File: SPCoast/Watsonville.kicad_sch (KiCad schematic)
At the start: 201 parts, among them SW15003 3, SW15005 5, SW15007 7, SW15009 9, SW15011 11, SW15013 13, SW15015 15, SW15017 17, SW15019 19, SW15021 21, SW15023 23, SW15025 25, SW15837 837

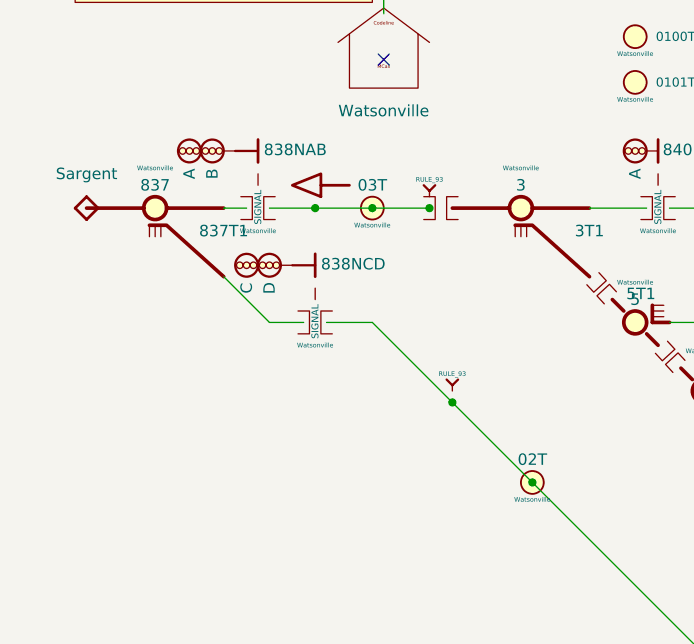
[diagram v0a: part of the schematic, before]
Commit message: feat(kicad): owner edit (2026-10-26): NextCP carries Interlocking; Industry carries Name; HBA leaves the track
The owner's edits after the trackplan review:
- NextCP gains Interlocking = ${Value}, a key the compiler reads for the destination; every instance takes it.
  Christopher's two NextCPs toward Corporal now say Corporal (both said Sargent).
- Industry gains Name = ${VALUE}. The five Industries are named: Gilroy Industry at Luchessa, Beet Loader 1
  and 2 at Corporal and at Sargent.
- Sargent's HBA (hot box alarm) is moved off 1SAT's net; its MC pin is unconnected and it carries Milepost 83.4.
- Watsonville: one Rule 93 (YARD) symbol is moved to the yard side of its joint.
Panels/ is left untracked.

Verified:
- Netlist exported by the owner 2026-10-26 12:37, newer than every sheet and the library.
- lint_symbol_fields: 100 symbols, 0 errors, 0 warnings.

Co-Authored-By: Claude Opus 5.5 <noreply@anthropic.com>
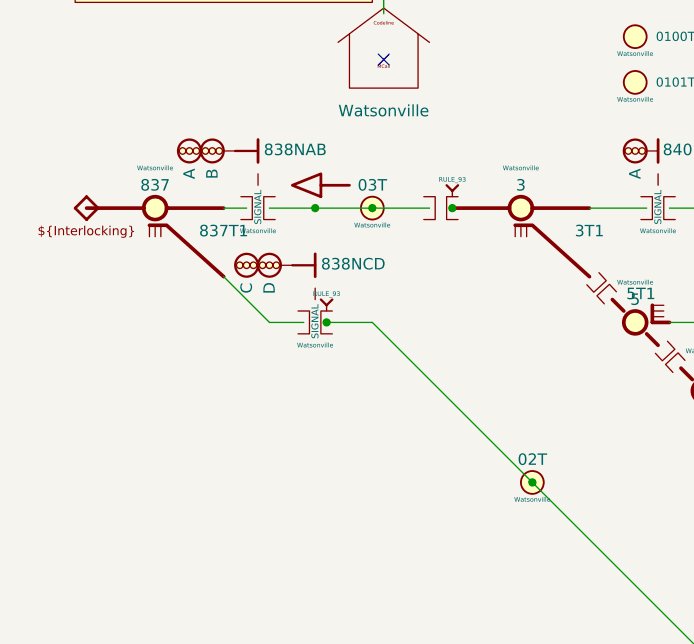
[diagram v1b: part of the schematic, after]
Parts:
- CP15001: Interlocking (none) -> ${Value}
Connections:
- net at B15003.2 (B), B15004.1 (A), DOT15004.1 (To)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: no longer DOT15001.1 (To)
- net at B15004.2 (B), SW15003.1 (C): now also DOT15001.1 (To)

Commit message: feat(kicad): owner edit (2026-10-27): Watsonville gets mast 838SAB on a new signal joint
The owner added the southbound 838SAB mast (a double mast with heads A and B), on
a new IRJ-Signal joint with CP Watsonville, closing the 838S TBD. The desk's 838
signal lever now has a field mast. The Sargent NextCP was redrawn, and
SPCoast.kicad_pro records the new designators.

Verified: only Watsonville.kicad_sch and SPCoast.kicad_pro changed. The added
symbols are Mast_Double 838SAB (Style double), heads A and B (CPL) and IRJ-Signal
B15005 (CP Watsonville); NextCP CP15001 (Sargent) is unchanged in its fields.
KiCad was closed (no lock files).

Co-Authored-By: Claude Opus 5.5 <noreply@anthropic.com>
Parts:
- added B15005: (no value), symbol Railroad-Trackplan:IRJ-Signal
- added H15013: A, symbol Railroad-Trackplan:Signal Head - CPL
- added H15014: B, symbol Railroad-Trackplan:Signal Head - CPL
- added S15011: 838SAB, symbol Railroad-Trackplan:Mast_Double
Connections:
- net at CP15001.1 (To): now also B15005.2 (B); no longer SW15837.1 (C)
- new net: H15014.1 (M), S15011.2 (H2)
- new net: B15005.1 (A), SW15837.1 (C)
- new net: H15013.1 (M), S15011.3 (H1)
- new net: B15005.3 (SIGNAL), S15011.1 (SIGNAL)

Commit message: refactor(symbols): the CP field is CP Name on every trackplan symbol
One fact, which house an appliance or circuit stands in, had two field
names: CP Name on the House and PanelColumn, CP on 17 trackplan
symbols. Every CP is now CP Name, in the library and in each placed
symbol, by a text rename of the field name only (KiCad's update
symbols was not used; it resets per-instance fields).

Verified: fresh kicad-cli netlists before and after: 754 components on
both, 136 had CP, every field identical once CP is read as CP Name, no
CP left. lint_symbol_fields: 100 symbols, 0 errors, 0 warnings.

Co-Authored-By: Claude Opus 5.5 <noreply@anthropic.com>
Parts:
- B15002, B15003, B15005, B15012, B15013, B15014, B15015, B15016, B15017, B15018, B15043, FLK15003, FLK15004, SW15003, SW15005, SW15007, SW15009, SW15011, SW15013, SW15015, SW15017, SW15019, SW15021, SW15023, SW15025, SW15837, TC15001, TC15002, TC15003, TC15004, TC15005, TC15006, TC15007, TC15008, TC15009, TC15010, TC15011, TC15012, TC15013, TC15014, TC15015, TC15016, TC15017, TC15018, TC15019, TC15020, TC15021, TC15022, TC15023, TC15024, TC15025, TC15026, TC15027, TC15028, TC15029, TC15030, TC15031, TC15032, TC15033, TC15034: CP Watsonville -> (none); CP Name (none) -> Watsonville
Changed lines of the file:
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@@
 			)
 		)
-		(property "CP" "Watsonville"
+		(property "CP Name" "Watsonville"
 			(at 222.25 79.375 0)
 			(show_name no)
@@
 			)
 		)
-		(property "CP" "Watsonville"
+		(property "CP Name" "Watsonville"
 			(at 81.28 37.465 0)
 			(show_name no)
@@
 			)
 		)
-		(property "CP" "Watsonville"
+		(property "CP Name" "Watsonville"
 			(at 167.64 76.835 0)
 			(show_name no)
@@
 			)
 		)
-		(property "CP" "Watsonville"
+		(property "CP Name" "Watsonville"
 			(at 137.16 107.315 0)
 			(show_name no)
@@
 			)
 		)
-		(property "CP" "Watsonville"
+		(property "CP Name" "Watsonville"
 			(at 167.64 56.515 0)
 			(show_name no)
@@
 			)
 		)
-		(property "CP" "Watsonville"
+		(property "CP Name" "Watsonville"
 			(at 68.58 50.165 0)
 			(show_name no)
@@
 			)
 		)
-		(property "CP" "Watsonville"
+		(property "CP Name" "Watsonville"
 			(at 39.37 57.15 0)
 			(show_name no)
@@
 			)
 		)
-		(property "CP" "Watsonville"
+		(property "CP Name" "Watsonville"
 			(at 116.84 92.71 0)
 			(show_name no)
@@
 			)
 		)
-		(property "CP" "Watsonville"
+		(property "CP Name" "Watsonville"
 			(at 147.32 56.515 0)
 			(show_name no)
@@
 			)
 		)
-		(property "CP" "Watsonville"
+		(property "CP Name" "Watsonville"
 			(at 45.72 69.85 0)
 			(show_name no)
@@
 			)
 		)
-		(property "CP" "Watsonville"
+		(property "CP Name" "Watsonville"
 			(at 237.49 94.615 0)
 			(show_name no)
@@
 			)
 		)
-		(property "CP" "Watsonville"
+		(property "CP Name" "Watsonville"
 			(at 137.16 56.515 0)
 			(show_name no)
@@
 			)
 		)
-		(property "CP" "Watsonville"
+		(property "CP Name" "Watsonville"
 			(at 81.28 62.865 0)
 			(show_name no)
@@
 			)
 		)
-		(property "CP" "Watsonville"
+		(property "CP Name" "Watsonville"
 			(at 52.07 56.515 0)
 			(show_name no)
@@
 			)
 		)
-		(property "CP" "Watsonville"
+		(property "CP Name" "Watsonville"
 			(at 147.32 92.075 0)
 			(show_name no)
@@
 			)
 		)
-		(property "CP" "Watsonville"
+		(property "CP Name" "Watsonville"
 			(at 205.74 69.215 0)
 			(show_name no)
@@
 			)
 		)
-		(property "CP" "Watsonville"
+		(property "CP Name" "Watsonville"
 			(at 137.16 76.835 0)
 			(show_name no)
@@
 			)
 		)
-		(property "CP" "Watsonville"
+		(property "CP Name" "Watsonville"
 			(at 157.48 107.315 0)
 			(show_name no)
@@
 			)
 		)
-		(property "CP" "Watsonville"
+		(property "CP Name" "Watsonville"
 			(at 157.48 92.075 0)
 			(show_name no)
@@
 			)
 		)
-		(property "CP" "Watsonville"
+		(property "CP Name" "Watsonville"
 			(at 109.22 85.09 0)
 			(show_name no)
@@
 			)
 		)
-		(property "CP" "Watsonville"
+		(property "CP Name" "Watsonville"
 			(at 111.76 93.345 0)
 			(show_name no)
@@
 			)
 		)
-		(property "CP" "Watsonville"
+		(property "CP Name" "Watsonville"
 			(at 157.48 56.515 0)
 			(show_name no)
@@
 			)
 		)
-		(property "CP" "Watsonville"
+		(property "CP Name" "Watsonville"
 			(at 101.6 77.47 0)
 			(show_name no)
@@
 			)
 		)
-		(property "CP" "Watsonville"
+		(property "CP Name" "Watsonville"
 			(at 147.32 107.315 0)
 			(show_name no)
@@
 			)
 		)
-		(property "CP" "Watsonville"
+		(property "CP Name" "Watsonville"
 			(at 81.28 42.545 0)
 			(show_name no)
@@
 			)
 		)
-		(property "CP" "Watsonville"
+		(property "CP Name" "Watsonville"
 			(at 69.85 86.995 0)
 			(show_name no)
@@
 			)
 		)
-		(property "CP" "Watsonville"
+		(property "CP Name" "Watsonville"
 			(at 243.84 115.57 0)
 			(show_name no)
@@
 			)
 		)
-		(property "CP" "Watsonville"
+		(property "CP Name" "Watsonville"
 			(at 157.48 84.455 0)
 			(show_name no)
@@
 			)
 		)
-		(property "CP" "Watsonville"
+		(property "CP Name" "Watsonville"
 			(at 96.52 78.105 0)
 			(show_name no)
@@
 			)
 		)
-		(property "CP" "Watsonville"
+		(property "CP Name" "Watsonville"
 			(at 167.64 92.075 0)
 			(show_name no)
@@
 			)
 		)
-		(property "CP" "Watsonville"
+		(property "CP Name" "Watsonville"
 			(at 147.32 69.215 0)
 			(show_name no)
@@
 			)
 		)
-		(property "CP" "Watsonville"
+		(property "CP Name" "Watsonville"
 			(at 229.87 86.995 0)
 			(show_name no)
@@
 			)
 		)
-		(property "CP" "Watsonville"
+		(property "CP Name" "Watsonville"
 			(at 167.64 84.455 0)
 			(show_name no)
@@
 			)
 		)
-		(property "CP" "Watsonville"
+		(property "CP Name" "Watsonville"
 			(at 137.16 69.215 0)
 			(show_name no)
@@
 			)
 		)
-		(property "CP" "Watsonville"
+		(property "CP Name" "Watsonville"
 			(at 147.32 84.455 0)
 			(show_name no)
@@
 			)
 		)
-		(property "CP" "Watsonville"
+		(property "CP Name" "Watsonville"
 			(at 83.82 57.15 0)
 			(show_name no)
@@
 			)
 		)
-		(property "CP" "Watsonville"
+		(property "CP Name" "Watsonville"
 			(at 157.48 99.695 0)
 			(show_name no)
@@
 			)
 		)
-		(property "CP" "Watsonville"
+		(property "CP Name" "Watsonville"
 			(at 147.32 76.835 0)
 			(show_name no)
@@
 			)
 		)
-		(property "CP" "Watsonville"
+		(property "CP Name" "Watsonville"
 			(at 167.64 69.215 0)
 			(show_name no)
@@
 			)
 		)
-		(property "CP" "Watsonville"
+		(property "CP Name" "Watsonville"
 			(at 88.9 70.485 0)
 			(show_name no)
@@
 			)
 		)
-		(property "CP" "Watsonville"
+		(property "CP Name" "Watsonville"
 			(at 149.86 33.02 0)
 			(show_name no)
@@
 			)
 		)
-		(property "CP" "Watsonville"
+		(property "CP Name" "Watsonville"
 			(at 167.64 120.015 0)
 			(show_name no)
@@
 			)
 		)
-		(property "CP" "Watsonville"
+		(property "CP Name" "Watsonville"
 			(at 130.81 107.95 0)
 			(show_name no)
@@
 			)
 		)
-		(property "CP" "Watsonville"
+		(property "CP Name" "Watsonville"
 			(at 137.16 99.695 0)
 			(show_name no)
@@
 			)
 		)
-		(property "CP" "Watsonville"
+		(property "CP Name" "Watsonville"
 			(at 252.73 109.855 0)
 			(show_name no)
@@
 			)
 		)
-		(property "CP" "Watsonville"
+		(property "CP Name" "Watsonville"
 			(at 167.64 99.695 0)
 			(show_name no)
@@
 			)
 		)
-		(property "CP" "Watsonville"
+		(property "CP Name" "Watsonville"
 			(at 156.21 33.02 0)
 			(show_name no)
@@
 			)
 		)
-		(property "CP" "Watsonville"
+		(property "CP Name" "Watsonville"
 			(at 137.16 92.075 0)
 			(show_name no)
@@
 			)
 		)
-		(property "CP" "Watsonville"
+		(property "CP Name" "Watsonville"
 			(at 93.98 69.85 0)
 			(show_name no)
@@
 			)
 		)
-		(property "CP" "Watsonville"
+		(property "CP Name" "Watsonville"
 			(at 147.32 99.695 0)
 			(show_name no)
@@
 			)
 		)
-		(property "CP" "Watsonville"
+		(property "CP Name" "Watsonville"
 			(at 137.16 84.455 0)
 			(show_name no)
@@
 			)
 		)
-		(property "CP" "Watsonville"
+		(property "CP Name" "Watsonville"
 			(at 167.64 107.315 0)
 			(show_name no)
@@
 			)
 		)
-		(property "CP" "Watsonville"
+		(property "CP Name" "Watsonville"
 			(at 245.11 102.235 0)
 			(show_name no)
@@
 			)
 		)
-		(property "CP" "Watsonville"
+		(property "CP Name" "Watsonville"
 			(at 27.94 50.165 0)
 			(show_name no)
@@
 			)
 		)
-		(property "CP" "Watsonville"
+		(property "CP Name" "Watsonville"
 			(at 124.46 100.33 0)
 			(show_name no)
@@
 			)
 		)
-		(property "CP" "Watsonville"
+		(property "CP Name" "Watsonville"
 			(at 189.23 71.755 0)
 			(show_name no)
@@
 			)
 		)
-		(property "CP" "Watsonville"
+		(property "CP Name" "Watsonville"
 			(at 104.14 85.725 0)
 			(show_name no)
@@
 			)
 		)
-		(property "CP" "Watsonville"
+		(property "CP Name" "Watsonville"
 			(at 19.05 52.07 0)
 			(show_name no)
@@
 			)
 		)
-		(property "CP" "Watsonville"
+		(property "CP Name" "Watsonville"
 			(at 157.48 69.215 0)
 			(show_name no)
@@
 			)
 		)
-		(property "CP" "Watsonville"
+		(property "CP Name" "Watsonville"
 			(at 157.48 76.835 0)
 			(show_name no)

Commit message: fix(spcoast): Watsonville's 842SA is 840SA, and the reverse loop is marked
The owner's edit in KiCad: the mast and its head device are renamed
842SA to 840SA, and a note marks the reverse-loop point where South
becomes North.

Verified: no 842SA left in the sheet; a fresh compile reports no
head.plan error.

Co-Authored-By: Claude Opus 5.5 <noreply@anthropic.com>
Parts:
- DevMast15009, S15010: value 842SA -> 840SA
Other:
- note added: "Reverse loop point: This is where South becomes North ==>"
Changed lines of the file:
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@@
 		)
 	)
+	(text "Reverse loop point:\nThis is where South becomes North ==>"
+		(exclude_from_sim no)
+		(at 236.22 112.268 0)
+		(effects
+			(font
+				(size 1.27 1.27)
+			)
+		)
+	)
 	(junction
 		(at 157.48 97.79)
@@
 			)
 		)
-		(property "Value" "842SA"
+		(property "Value" "840SA"
 			(at 34.29 156.21 0)
 			(hide yes)
@@
 			)
 		)
-		(property "Value" "842SA"
+		(property "Value" "840SA"
 			(at 243.332 124.587 0)
 			(show_name no)

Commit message: feat(symbols,spcoast): track circuits state their Indication; virtual circuits list Members
The owner's edit, 2026-10-29. Every Track Circuit symbol (plain, RED,
Yellow, Virtual) carries Indication=${Name}K: the token a local circuit
reports and a remote consumer (Sargent's Corporal:2NAT) consumes, so
both sides state it and match token to token. Track Circuit_Virtual's
IndicationToken becomes Members (the local circuits it is made of, not
tokens), with Display=${Value}: [${Members}]. Sargent's HBA gets a
no-connect on its unused pin. The panel sheets are re-saved by KiCad
with no field changes.

Verified:
- netlist field diff against 69e87ec: 747 components, none added or
  removed; the only changes are Indication added on 63 track circuits
  (26 Track Circuit, 35 Yellow, 2 Virtual) and IndicationToken renamed
  to Members on TC15032 and TC15034
- ERC: 0 violations (was 1, Sargent AUX1 pin_not_connected)
- Subdivision lint_symbol_fields: 100 symbols, 0 errors, 0 warnings
- Subdivision fresh compile: 0 errors, 0 warnings, 8 info, 2 missing;
  consumer.legacy_token no longer fires

Co-Authored-By: Claude Opus 5.5 <noreply@anthropic.com>
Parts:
- TC15001, TC15002, TC15003, TC15004, TC15005, TC15006, TC15007, TC15008, TC15009, TC15010, TC15011, TC15012, TC15013, TC15014, TC15015, TC15016, TC15017, TC15018, TC15019, TC15020, TC15021, TC15022, TC15023, TC15024, TC15025, TC15026, TC15027, TC15028, TC15029, TC15030, TC15031, TC15033: Indication (none) -> ${Name}K
- TC15032: Display ${Value}: [${IndicationToken}] -> ${Value}: [${Members}]; Indication (none) -> ${Name}K; IndicationToken 15T1,17T1,19T1,21T1,23T1,25T1 -> (none); Members (none) -> 15T1,17T1,19T1,21T1,23T1,25T1
- TC15034: Display ${Value}: [${IndicationToken}] -> ${Value}: [${Members}]; Indication (none) -> ${Name}K; IndicationToken 03T,3T1,5T1,7T1,9T1,11T1,13T1 -> (none); Members (none) -> 03T,3T1,5T1,7T1,9T1,11T1,13T1

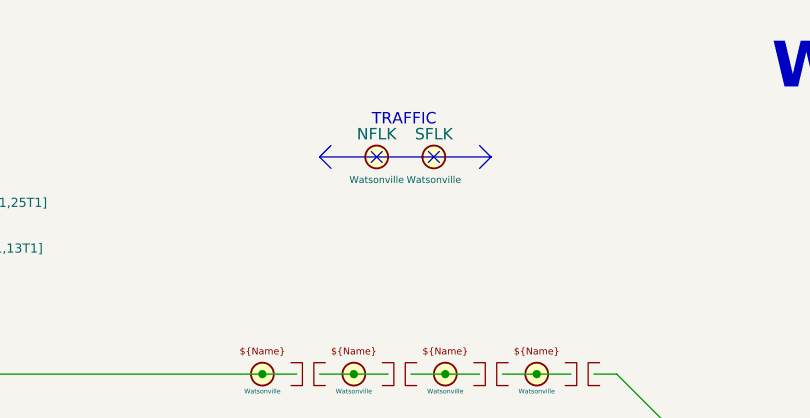
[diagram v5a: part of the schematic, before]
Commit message: feat(symbols): switches and field lamps state their indication token
A switch states its OS circuit's token, Indication=${TC}K, on Switch_Dual,
Switch_Lock, Switch_Powered, Switch_Powered_Diag, Switch_Powered_Small and
Derail_TC; symbols with no TC (Derail, Switch_Manual, Switch_Manual_Sensed,
Switch_Powered_NO_TC) carry the field present and empty. The AUXILIARY field
lamp states Indication=${Name}K. The four NFLK/SFLK lamps in Luchessa and
Watsonville are renamed NFL/SFL, so their tokens stay NFLK/SFLK. The
sheets are updated from the library.

Verified:
- fresh kicad-cli netlist vs HEAD 6ce30b3: 747 components each, 46 field
  changes: 31 switch/derail Indication, HBA Indication=HBAK, the four
  NFL/SFL renames with their Indication, and MC5001's library entry name
  (MaintainerCall_1 -> MaintainerCall); nothing else
- kicad-cli ERC: 0 violations
- tools/contract/lint_symbol_fields.py: 100 symbols, 0 errors, 0 warnings
- compile_layout.py: 0 errors, 0 warnings, 8 info, 2 missing (unchanged)

Co-Authored-By: Claude Opus 5.5 <noreply@anthropic.com>
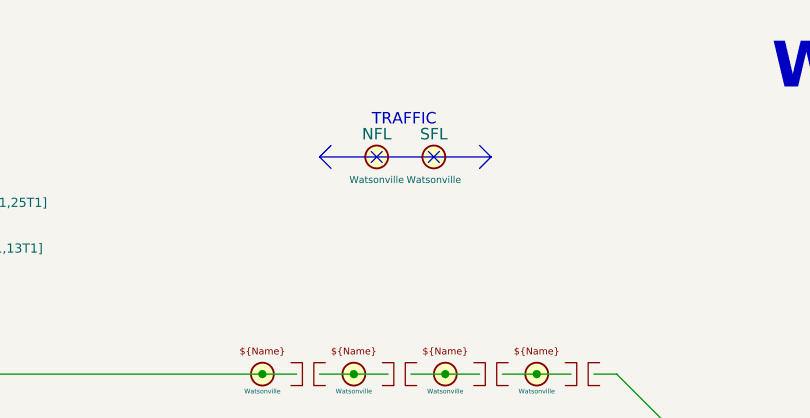
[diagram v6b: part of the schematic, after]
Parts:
- FLK15003: value NFLK -> NFL; Indication (none) -> ${Name}K
- FLK15004: value SFLK -> SFL; Indication (none) -> ${Name}K
- SW15003, SW15005, SW15007, SW15009, SW15011, SW15013, SW15015, SW15017, SW15019, SW15021, SW15023, SW15025, SW15837: Indication (none) -> ${TC}K
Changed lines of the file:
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@@
 			)
 		)
+		(property "Indication" "${TC}K"
+			(at 222.25 74.93 0)
+			(hide yes)
+			(show_name no)
+			(do_not_autoplace no)
+			(effects
+				(font
+					(size 1.27 1.27)
+				)
+			)
+		)
 		(pin "2"
 		)
@@
 			)
 		)
+		(property "Indication" "${TC}K"
+			(at 68.58 54.61 0)
+			(hide yes)
+			(show_name no)
+			(do_not_autoplace no)
+			(effects
+				(font
+					(size 1.27 1.27)
+				)
+			)
+		)
 		(pin "2"
 		)
@@
 			)
 		)
+		(property "Indication" "${TC}K"
+			(at 237.49 90.17 0)
+			(hide yes)
+			(show_name no)
+			(do_not_autoplace no)
+			(effects
+				(font
+					(size 1.27 1.27)
+				)
+			)
+		)
 		(pin "2"
 		)
@@
 			)
 		)
+		(property "Indication" "${TC}K"
+			(at 81.28 67.31 0)
+			(hide yes)
+			(show_name no)
+			(do_not_autoplace no)
+			(effects
+				(font
+					(size 1.27 1.27)
+				)
+			)
+		)
 		(pin "2"
 		)
@@
 			)
 		)
+		(property "Indication" "${TC}K"
+			(at 111.76 97.79 0)
+			(hide yes)
+			(show_name no)
+			(do_not_autoplace no)
+			(effects
+				(font
+					(size 1.27 1.27)
+				)
+			)
+		)
 		(pin "2"
 		)
@@
 			)
 		)
+		(property "Indication" "${TC}K"
+			(at 96.52 82.55 0)
+			(hide yes)
+			(show_name no)
+			(do_not_autoplace no)
+			(effects
+				(font
+					(size 1.27 1.27)
+				)
+			)
+		)
 		(pin "2"
 		)
@@
 			)
 		)
+		(property "Indication" "${TC}K"
+			(at 229.87 82.55 0)
+			(hide yes)
+			(show_name no)
+			(do_not_autoplace no)
+			(effects
+				(font
+					(size 1.27 1.27)
+				)
+			)
+		)
 		(pin "2"
 		)
@@
 			)
 		)
+		(property "Indication" "${TC}K"
+			(at 88.9 74.93 0)
+			(hide yes)
+			(show_name no)
+			(do_not_autoplace no)
+			(effects
+				(font
+					(size 1.27 1.27)
+				)
+			)
+		)
 		(pin "2"
 		)
@@
 			)
 		)
-		(property "Value" "NFLK"
+		(property "Value" "NFL"
 			(at 149.86 27.94 0)
 			(show_name no)
@@
 			)
 		)
+		(property "Indication" "${Name}K"
+			(at 149.86 30.48 0)
+			(hide yes)
+			(show_name no)
+			(do_not_autoplace no)
+			(effects
+				(font
+					(size 1.27 1.27)
+				)
+			)
+		)
 		(pin "1"
 		)
@@
 			)
 		)
+		(property "Indication" "${TC}K"
+			(at 252.73 105.41 0)
+			(hide yes)
+			(show_name no)
+			(do_not_autoplace no)
+			(effects
+				(font
+					(size 1.27 1.27)
+				)
+			)
+		)
 		(pin "2"
 		)
@@
 			)
 		)
-		(property "Value" "SFLK"
+		(property "Value" "SFL"
 			(at 156.21 27.94 0)
 			(show_name no)
@@
 			)
 		)
+		(property "Indication" "${Name}K"
+			(at 156.21 30.48 0)
+			(hide yes)
+			(show_name no)
+			(do_not_autoplace no)
+			(effects
+				(font
+					(size 1.27 1.27)
+				)
+			)
+		)
 		(pin "1"
 		)
@@
 			)
 		)
+		(property "Indication" "${TC}K"
+			(at 245.11 97.79 0)
+			(hide yes)
+			(show_name no)
+			(do_not_autoplace no)
+			(effects
+				(font
+					(size 1.27 1.27)
+				)
+			)
+		)
 		(pin "2"
 		)
@@
 			)
 		)
+		(property "Indication" "${TC}K"
+			(at 27.94 54.61 0)
+			(hide yes)
+			(show_name no)
+			(do_not_autoplace no)
+			(effects
+				(font
+					(size 1.27 1.27)
+				)
+			)
+		)
 		(pin "2"
 		)
@@
 			)
 		)
+		(property "Indication" "${TC}K"
+			(at 189.23 67.31 0)
+			(hide yes)
+			(show_name no)
+			(do_not_autoplace no)
+			(effects
+				(font
+					(size 1.27 1.27)
+				)
+			)
+		)
 		(pin "2"
 		)
@@
 			(hide yes)
 			(show_name no)
+			(do_not_autoplace no)
+			(effects
+				(font
+					(size 1.27 1.27)
+				)
+			)
+		)
+		(property "Indication" "${TC}K"
+			(at 104.14 90.17 0)
+			(hide yes)
+			(show_name no)

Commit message: fix(symbols): AUXILIARY field lamp drops Style=non_vital
Vital is an attribute of a control token on a code line; no indication is
vital, so the field lamp's Style=non_vital meant nothing, and no code read
it. Removed from the library symbol and the five instances.

Verified:
- fresh kicad-cli netlist vs HEAD 13f7ecd: 747 components each; the only
  field changes are Style removed on HBA, NFL and SFL (Luchessa and
  Watsonville)
- kicad-cli ERC: 0 violations
- tools/contract/lint_symbol_fields.py: 100 symbols, 0 errors, 0 warnings

Co-Authored-By: Claude Opus 5.5 <noreply@anthropic.com>
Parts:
- FLK15003, FLK15004: Style non_vital -> (none)
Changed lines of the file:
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@@
-			)
-		)
-		(property "Style" "non_vital"
-			(at 149.86 30.48 0)
-			(hide yes)
-			(show_name no)
-			(do_not_autoplace no)
-			(effects
-				(font
-					(size 1.27 1.27)
-				)
 			)
 		)
@@
 			(at 156.21 30.48 0)
 			(hide yes)
-			(show_name no)
-			(do_not_autoplace no)
-			(effects
-				(font
-					(size 1.27 1.27)
-				)
-			)
-		)
-		(property "Style" "non_vital"
-			(at 156.21 30.48 0)
-			(hide yes)
